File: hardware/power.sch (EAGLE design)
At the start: 31 parts, among them IC3 LM2937, U1 LM324D, U2 LM324D

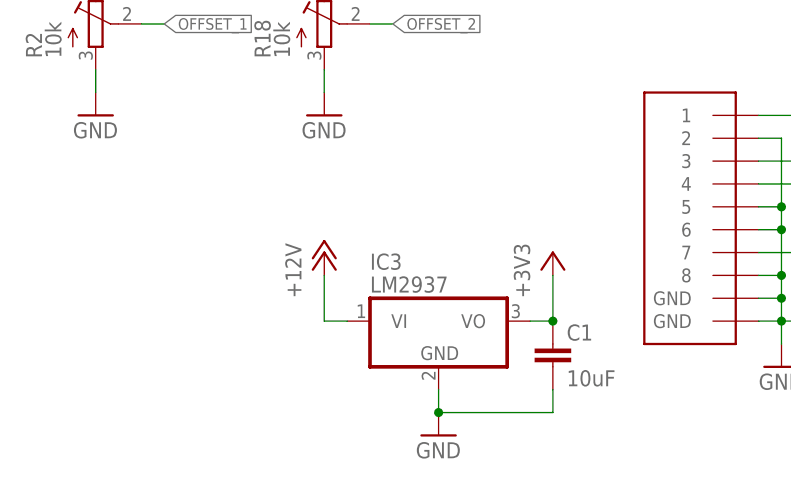
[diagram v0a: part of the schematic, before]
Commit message: preliminary placement and routing
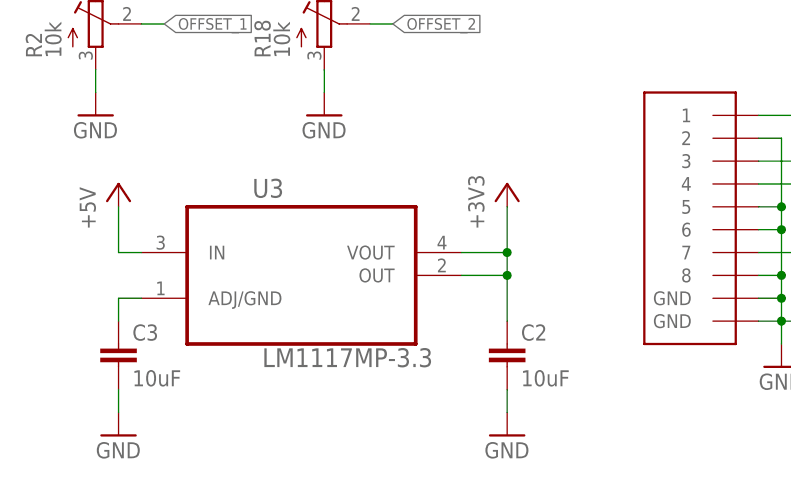
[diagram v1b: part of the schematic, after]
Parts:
- removed C1: 10uF, rcl:C-EUC0805
- removed IC3: LM2937, linear:LM2937
- added C2, C3: 10uF, rcl:C-EUC0805
- added U3: LM1117MP-3.3, hexasense:LM1117MP-3.3
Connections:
- removed net +12V: IC3.VI, U$2.I
- new net N$15: C3.1, U3.ADJ/GND
- net +3V3: now also C2.1, U3.OUT, U3.VOUT; no longer C1.1, IC3.VO
- net +5V: now also U$2.I, U3.IN
- net GND: now also C2.2, C3.2; no longer C1.2, IC3.GND
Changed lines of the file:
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@@
 <part name="GND1" library="supply1" deviceset="GND" device=""/>
 <part name="GND2" library="supply1" deviceset="GND" device=""/>
-<part name="GND3" library="supply1" deviceset="GND" device=""/>
 <part name="GND4" library="supply1" deviceset="GND" device=""/>
-<part name="IC3" library="linear" deviceset="LM2937" device=""/>
-<part name="+3V3" library="supply1" deviceset="+3V3" device=""/>
-<part name="P+1" library="supply1" deviceset="+12V" device=""/>
 <part name="R2" library="rcl" deviceset="R-TRIMM" device="T93YB" value="10k"/>
 <part name="R4" library="rcl" deviceset="R-TRIMM" device="T93YB" value="20k"/>
@@
 <part name="TP4" library="testpad" deviceset="TP" device="B1,27"/>
 <part name="U$2" library="Ergaenzung" deviceset="HOHLBUCHSE" device=""/>
-<part name="P+2" library="supply1" deviceset="+5V" device=""/>
 <part name="GND8" library="supply1" deviceset="GND" device=""/>
 <part name="+3V5" library="supply1" deviceset="+3V3" device=""/>
 <part name="JP2" library="pinhead" deviceset="PINHD-1X4" device="/90"/>
-<part name="C1" library="rcl" deviceset="C-EU" device="C0805" value="10uF"/>
 <part name="U1" library="hexasense" deviceset="LM324D" device=""/>
 <part name="+3V4" library="supply1" deviceset="+3V3" device=""/>
@@
 <part name="GND13" library="supply1" deviceset="GND" device=""/>
 <part name="P+3" library="supply1" deviceset="+5V" device=""/>
+<part name="U3" library="hexasense" deviceset="LM1117MP-3.3" device=""/>
+<part name="P+4" library="supply1" deviceset="+5V" device=""/>
+<part name="+3V9" library="supply1" deviceset="+3V3" device=""/>
+<part name="GND7" library="supply1" deviceset="GND" device=""/>
+<part name="GND14" library="supply1" deviceset="GND" device=""/>
+<part name="C2" library="rcl" deviceset="C-EU" device="C0805" value="10uF"/>
+<part name="C3" library="rcl" deviceset="C-EU" device="C0805" value="10uF"/>
+<part name="P+1" library="supply1" deviceset="+5V" device=""/>
 </parts>
 <sheets>
@@
 <instance part="GND1" gate="1" x="58.42" y="55.88"/>
 <instance part="GND2" gate="1" x="147.32" y="53.34"/>
-<instance part="GND3" gate="1" x="43.18" y="-2.54"/>
 <instance part="GND4" gate="1" x="10.16" y="76.2"/>
-<instance part="IC3" gate="G$1" x="43.18" y="10.16"/>
-<instance part="+3V3" gate="G$1" x="55.88" y="17.78"/>
-<instance part="P+1" gate="1" x="30.48" y="17.78"/>
 <instance part="R2" gate="G$1" x="5.08" y="43.18"/>
 <instance part="R4" gate="G$1" x="147.32" y="63.5" rot="R180"/>
@@
 <instance part="TP4" gate="G$1" x="83.82" y="38.1"/>
 <instance part="U$2" gate="G$1" x="129.54" y="38.1" rot="R180"/>
-<instance part="P+2" gate="1" x="114.3" y="45.72"/>
 <instance part="GND8" gate="1" x="114.3" y="30.48"/>
 <instance part="+3V5" gate="G$1" x="91.44" y="38.1"/>
 <instance part="JP2" gate="A" x="0" y="86.36" rot="R180"/>
-<instance part="C1" gate="G$1" x="55.88" y="7.62"/>
 <instance part="U1" gate="A" x="109.22" y="83.82"/>
 <instance part="+3V4" gate="G$1" x="91.44" y="111.76"/>
@@
 <instance part="GND13" gate="1" x="30.48" y="33.02"/>
 <instance part="P+3" gate="1" x="91.44" y="22.86"/>
+<instance part="U3" gate="A" x="27.94" y="17.78"/>
+<instance part="P+4" gate="1" x="7.62" y="25.4"/>
+<instance part="+3V9" gate="G$1" x="50.8" y="25.4"/>
+<instance part="GND7" gate="1" x="7.62" y="-2.54"/>
+<instance part="GND14" gate="1" x="50.8" y="-2.54"/>
+<instance part="C2" gate="G$1" x="50.8" y="7.62"/>
+<instance part="C3" gate="G$1" x="7.62" y="7.62"/>
+<instance part="P+1" gate="1" x="114.3" y="45.72"/>
 </instances>
 <busses>
@@
 <pinref part="R3" gate="G$1" pin="2"/>
 <pinref part="+3V2" gate="G$1" pin="+3V3"/>
-</segment>
-<segment>
-<wire x1="53.34" y1="10.16" x2="55.88" y2="10.16" width="0.1524" layer="91"/>
-<wire x1="55.88" y1="10.16" x2="55.88" y2="15.24" width="0.1524" layer="91"/>
-<junction x="55.88" y="10.16"/>
-<pinref part="IC3" gate="G$1" pin="VO"/>
-<pinref part="+3V3" gate="G$1" pin="+3V3"/>
-<pinref part="C1" gate="G$1" pin="1"/>
 </segment>
 <segment>
@@
 <pinref part="+3V8" gate="G$1" pin="+3V3"/>
 </segment>
+<segment>
+<pinref part="U3" gate="A" pin="VOUT"/>
+<pinref part="+3V9" gate="G$1" pin="+3V3"/>
+<wire x1="45.72" y1="17.78" x2="50.8" y2="17.78" width="0.1524" layer="91"/>
+<wire x1="50.8" y1="17.78" x2="50.8" y2="22.86" width="0.1524" layer="91"/>
+<pinref part="U3" gate="A" pin="OUT"/>
+<wire x1="45.72" y1="15.24" x2="50.8" y2="15.24" width="0.1524" layer="91"/>
+<wire x1="50.8" y1="15.24" x2="50.8" y2="17.78" width="0.1524" layer="91"/>
+<junction x="50.8" y="17.78"/>
+<pinref part="C2" gate="G$1" pin="1"/>
+<wire x1="50.8" y1="15.24" x2="50.8" y2="10.16" width="0.1524" layer="91"/>
+<junction x="50.8" y="15.24"/>
+</segment>
 </net>
 <net name="GND" class="0">
@@
 <pinref part="R5" gate="G$1" pin="1"/>
 <pinref part="GND1" gate="1" pin="GND"/>
-</segment>
-<segment>
-<wire x1="43.18" y1="0" x2="43.18" y2="2.54" width="0.1524" layer="91"/>
-<wire x1="55.88" y1="2.54" x2="55.88" y2="0" width="0.1524" layer="91"/>
-<wire x1="55.88" y1="0" x2="43.18" y2="0" width="0.1524" layer="91"/>
-<junction x="43.18" y="0"/>
-<pinref part="IC3" gate="G$1" pin="GND"/>
-<pinref part="GND3" gate="1" pin="GND"/>
-<pinref part="C1" gate="G$1" pin="2"/>
 </segment>
 <segment>
@@
 <pinref part="R18" gate="G$1" pin="A"/>
 </segment>
-</net>
-<net name="+12V" class="0">
-<segment>
-<wire x1="33.02" y1="10.16" x2="30.48" y2="10.16" width="0.1524" layer="91"/>
-<wire x1="30.48" y1="10.16" x2="30.48" y2="15.24" width="0.1524" layer="91"/>
-<pinref part="IC3" gate="G$1" pin="VI"/>
-<pinref part="P+1" gate="1" pin="+12V"/>
-</segment>
-<segment>
-<wire x1="116.84" y1="40.64" x2="114.3" y2="40.64" width="0.1524" layer="91"/>
-<wire x1="114.3" y1="40.64" x2="114.3" y2="43.18" width="0.1524" layer="91"/>
-<pinref part="U$2" gate="G$1" pin="I"/>
-<pinref part="P+2" gate="1" pin="+5V"/>
+<segment>
+<pinref part="C2" gate="G$1" pin="2"/>
+<pinref part="GND14" gate="1" pin="GND"/>
+<wire x1="50.8" y1="2.54" x2="50.8" y2="0" width="0.1524" layer="91"/>
+</segment>
+<segment>
+<pinref part="GND7" gate="1" pin="GND"/>
+<pinref part="C3" gate="G$1" pin="2"/>
+<wire x1="7.62" y1="0" x2="7.62" y2="2.54" width="0.1524" layer="91"/>
 </segment>
 </net>
@@
 <wire x1="91.44" y1="17.78" x2="91.44" y2="20.32" width="0.1524" layer="91"/>
 </segment>
-</net>
+<segment>
+<pinref part="U3" gate="A" pin="IN"/>
+<pinref part="P+4" gate="1" pin="+5V"/>
+<wire x1="10.16" y1="17.78" x2="7.62" y2="17.78" width="0.1524" layer="91"/>
+<wire x1="7.62" y1="17.78" x2="7.62" y2="22.86" width="0.1524" layer="91"/>
+</segment>
+<segment>
+<pinref part="U$2" gate="G$1" pin="I"/>
+<pinref part="P+1" gate="1" pin="+5V"/>
+<wire x1="116.84" y1="40.64" x2="114.3" y2="40.64" width="0.1524" layer="91"/>
+<wire x1="114.3" y1="40.64" x2="114.3" y2="43.18" width="0.1524" layer="91"/>
+</segment>
+</net>
+<net name="N$15" class="0">
+<segment>
+<pinref part="U3" gate="A" pin="ADJ/GND"/>
+<pinref part="C3" gate="G$1" pin="1"/>
+<wire x1="10.16" y1="12.7" x2="7.62" y2="12.7" width="0.1524" layer="91"/>
+<wire x1="7.62" y1="12.7" x2="7.62" y2="10.16" width="0.1524" layer="91"/>
+</segment>
+</net>

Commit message: now passing the DRC
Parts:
- added OFFSET-1, OFFSET-2, PT100-1, PT100-2: TPB1,27, testpad:TPB1,27
- renumbered C3 to C1, TP1 to U_M-1, TP2 to TEMP-1, TP3 to GND, TP4 to VCC, TP5 to U_M-2, TP6 to TEMP-2
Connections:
- net OFFSET_1: now also OFFSET-1.TP
- net OFFSET_2: now also OFFSET-2.TP
- net PT100_1: now also PT100-1.TP
- net PT100_2: now also PT100-2.TP
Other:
- moved on the sheet: JP2
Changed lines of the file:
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@@
 <part name="U$1" library="Reichelt" deviceset="MEBP8-8G" device=""/>
 <part name="GND6" library="supply1" deviceset="GND" device=""/>
-<part name="TP1" library="testpad" deviceset="TP" device="B1,27"/>
-<part name="TP2" library="testpad" deviceset="TP" device="B1,27"/>
-<part name="TP3" library="testpad" deviceset="TP" device="B1,27"/>
-<part name="TP4" library="testpad" deviceset="TP" device="B1,27"/>
+<part name="U_M-1" library="testpad" deviceset="TP" device="B1,27"/>
+<part name="TEMP-1" library="testpad" deviceset="TP" device="B1,27"/>
+<part name="GND" library="testpad" deviceset="TP" device="B1,27"/>
+<part name="VCC" library="testpad" deviceset="TP" device="B1,27"/>
 <part name="U$2" library="Ergaenzung" deviceset="HOHLBUCHSE" device=""/>
 <part name="GND8" library="supply1" deviceset="GND" device=""/>
@@
 <part name="GND11" library="supply1" deviceset="GND" device=""/>
 <part name="R16" library="rcl" deviceset="R-TRIMM" device="T93YB" value="20k"/>
-<part name="TP5" library="testpad" deviceset="TP" device="B1,27"/>
-<part name="TP6" library="testpad" deviceset="TP" device="B1,27"/>
+<part name="U_M-2" library="testpad" deviceset="TP" device="B1,27"/>
+<part name="TEMP-2" library="testpad" deviceset="TP" device="B1,27"/>
 <part name="U2" library="hexasense" deviceset="LM324D" device=""/>
 <part name="+3V7" library="supply1" deviceset="+3V3" device=""/>
@@
 <part name="GND14" library="supply1" deviceset="GND" device=""/>
 <part name="C2" library="rcl" deviceset="C-EU" device="C0805" value="10uF"/>
-<part name="C3" library="rcl" deviceset="C-EU" device="C0805" value="10uF"/>
+<part name="C1" library="rcl" deviceset="C-EU" device="C0805" value="10uF"/>
 <part name="P+1" library="supply1" deviceset="+5V" device=""/>
+<part name="OFFSET-1" library="testpad" deviceset="TP" device="B1,27"/>
+<part name="OFFSET-2" library="testpad" deviceset="TP" device="B1,27"/>
+<part name="PT100-2" library="testpad" deviceset="TP" device="B1,27"/>
+<part name="PT100-1" library="testpad" deviceset="TP" device="B1,27"/>
 </parts>
 <sheets>
@@
 <instance part="GND1" gate="1" x="58.42" y="55.88"/>
 <instance part="GND2" gate="1" x="147.32" y="53.34"/>
-<instance part="GND4" gate="1" x="10.16" y="76.2"/>
+<instance part="GND4" gate="1" x="0" y="78.74"/>
 <instance part="R2" gate="G$1" x="5.08" y="43.18"/>
 <instance part="R4" gate="G$1" x="147.32" y="63.5" rot="R180"/>
@@
 <instance part="U$1" gate="G$1" x="71.12" y="22.86"/>
 <instance part="GND6" gate="1" x="81.28" y="5.08"/>
-<instance part="TP1" gate="G$1" x="134.62" y="99.06"/>
-<instance part="TP2" gate="G$1" x="147.32" y="99.06"/>
-<instance part="TP3" gate="G$1" x="93.98" y="15.24"/>
-<instance part="TP4" gate="G$1" x="83.82" y="38.1"/>
+<instance part="U_M-1" gate="G$1" x="134.62" y="99.06"/>
+<instance part="TEMP-1" gate="G$1" x="147.32" y="99.06"/>
+<instance part="GND" gate="G$1" x="93.98" y="15.24"/>
+<instance part="VCC" gate="G$1" x="83.82" y="38.1"/>
 <instance part="U$2" gate="G$1" x="129.54" y="38.1" rot="R180"/>
 <instance part="GND8" gate="1" x="114.3" y="30.48"/>
 <instance part="+3V5" gate="G$1" x="91.44" y="38.1"/>
-<instance part="JP2" gate="A" x="0" y="86.36" rot="R180"/>
+<instance part="JP2" gate="A" x="-10.16" y="88.9" rot="R180"/>
 <instance part="U1" gate="A" x="109.22" y="83.82"/>
 <instance part="+3V4" gate="G$1" x="91.44" y="111.76"/>
@@
 <instance part="GND11" gate="1" x="147.32" y="124.46"/>
 <instance part="R16" gate="G$1" x="147.32" y="134.62" rot="R180"/>
-<instance part="TP5" gate="G$1" x="134.62" y="170.18"/>
-<instance part="TP6" gate="G$1" x="147.32" y="170.18"/>
+<instance part="U_M-2" gate="G$1" x="134.62" y="170.18"/>
+<instance part="TEMP-2" gate="G$1" x="147.32" y="170.18"/>
 <instance part="U2" gate="A" x="109.22" y="154.94"/>
 <instance part="+3V7" gate="G$1" x="91.44" y="182.88"/>
@@
 <instance part="GND14" gate="1" x="50.8" y="-2.54"/>
 <instance part="C2" gate="G$1" x="50.8" y="7.62"/>
-<instance part="C3" gate="G$1" x="7.62" y="7.62"/>
+<instance part="C1" gate="G$1" x="7.62" y="7.62"/>
 <instance part="P+1" gate="1" x="114.3" y="45.72"/>
+<instance part="OFFSET-1" gate="G$1" x="12.7" y="50.8"/>
+<instance part="OFFSET-2" gate="G$1" x="38.1" y="50.8"/>
+<instance part="PT100-2" gate="G$1" x="2.54" y="93.98"/>
+<instance part="PT100-1" gate="G$1" x="7.62" y="93.98"/>
 </instances>
 <busses>
@@
 <wire x1="83.82" y1="33.02" x2="83.82" y2="35.56" width="0.1524" layer="91"/>
 <junction x="83.82" y="33.02"/>
-<pinref part="TP4" gate="G$1" pin="TP"/>
+<pinref part="VCC" gate="G$1" pin="TP"/>
 <pinref part="U$1" gate="G$1" pin="1"/>
 <pinref part="+3V5" gate="G$1" pin="+3V3"/>
@@
 </segment>
 <segment>
-<wire x1="10.16" y1="78.74" x2="10.16" y2="83.82" width="0.1524" layer="91"/>
-<wire x1="10.16" y1="83.82" x2="10.16" y2="88.9" width="0.1524" layer="91"/>
-<wire x1="10.16" y1="88.9" x2="2.54" y2="88.9" width="0.1524" layer="91"/>
-<wire x1="2.54" y1="83.82" x2="10.16" y2="83.82" width="0.1524" layer="91"/>
-<junction x="10.16" y="83.82"/>
+<wire x1="0" y1="81.28" x2="0" y2="86.36" width="0.1524" layer="91"/>
+<wire x1="0" y1="86.36" x2="0" y2="91.44" width="0.1524" layer="91"/>
+<wire x1="0" y1="91.44" x2="-7.62" y2="91.44" width="0.1524" layer="91"/>
+<wire x1="-7.62" y1="86.36" x2="0" y2="86.36" width="0.1524" layer="91"/>
+<junction x="0" y="86.36"/>
 <pinref part="JP2" gate="A" pin="4"/>
 <pinref part="GND4" gate="1" pin="GND"/>
@@
 <wire x1="78.74" y1="20.32" x2="81.28" y2="20.32" width="0.1524" layer="91"/>
 <junction x="81.28" y="20.32"/>
-<pinref part="TP3" gate="G$1" pin="TP"/>
+<pinref part="GND" gate="G$1" pin="TP"/>
 <wire x1="93.98" y1="12.7" x2="93.98" y2="10.16" width="0.1524" layer="91"/>
 <wire x1="93.98" y1="10.16" x2="81.28" y2="10.16" width="0.1524" layer="91"/>
@@
 <segment>
 <pinref part="GND7" gate="1" pin="GND"/>
-<pinref part="C3" gate="G$1" pin="2"/>
+<pinref part="C1" gate="G$1" pin="2"/>
 <wire x1="7.62" y1="0" x2="7.62" y2="2.54" width="0.1524" layer="91"/>
 </segment>
@@
 </segment>
 <segment>
-<wire x1="2.54" y1="86.36" x2="12.7" y2="86.36" width="0.1524" layer="91"/>
-<label x="12.7" y="86.36" size="1.27" layer="95" xref="yes"/>
+<wire x1="-7.62" y1="88.9" x2="2.54" y2="88.9" width="0.1524" layer="91"/>
+<label x="10.16" y="88.9" size="1.27" layer="95" xref="yes"/>
 <pinref part="JP2" gate="A" pin="3"/>
+<pinref part="PT100-2" gate="G$1" pin="TP"/>
+<wire x1="2.54" y1="88.9" x2="10.16" y2="88.9" width="0.1524" layer="91"/>
+<wire x1="2.54" y1="91.44" x2="2.54" y2="88.9" width="0.1524" layer="91"/>
+<junction x="2.54" y="88.9"/>
 </segment>
 </net>
@@
 <label x="12.7" y="43.18" size="1.27" layer="95" xref="yes"/>
 <pinref part="R2" gate="G$1" pin="S"/>
+<pinref part="OFFSET-1" gate="G$1" pin="TP"/>
+<wire x1="12.7" y1="43.18" x2="12.7" y2="48.26" width="0.1524" layer="91"/>
 </segment>
 <segment>
@@
 <label x="38.1" y="43.18" size="1.27" layer="95" xref="yes"/>
 <pinref part="R18" gate="G$1" pin="S"/>
+<pinref part="OFFSET-2" gate="G$1" pin="TP"/>
+<wire x1="38.1" y1="43.18" x2="38.1" y2="48.26" width="0.1524" layer="91"/>
 </segment>
 <segment>
@@
 <net name="PT100_1" class="0">
 <segment>
-<wire x1="2.54" y1="81.28" x2="12.7" y2="81.28" width="0.1524" layer="91"/>
-<label x="12.7" y="81.28" size="1.27" layer="95" xref="yes"/>
+<wire x1="-7.62" y1="83.82" x2="7.62" y2="83.82" width="0.1524" layer="91"/>
+<label x="10.16" y="83.82" size="1.27" layer="95" xref="yes"/>
 <pinref part="JP2" gate="A" pin="1"/>
+<pinref part="PT100-1" gate="G$1" pin="TP"/>
+<wire x1="7.62" y1="83.82" x2="10.16" y2="83.82" width="0.1524" layer="91"/>
+<wire x1="7.62" y1="91.44" x2="7.62" y2="83.82" width="0.1524" layer="91"/>
+<junction x="7.62" y="83.82"/>
 </segment>
 <segment>
@@
 <label x="139.7" y="160.02" size="1.27" layer="95" xref="yes"/>
 <pinref part="U2" gate="A" pin="OUT3"/>
-<pinref part="TP5" gate="G$1" pin="TP"/>
+<pinref part="U_M-2" gate="G$1" pin="TP"/>
 </segment>
 <segment>
@@
 <label x="139.7" y="88.9" size="1.27" layer="95" xref="yes"/>
 <pinref part="U1" gate="A" pin="OUT3"/>
-<pinref part="TP1" gate="G$1" pin="TP"/>
+<pinref part="U_M-1" gate="G$1" pin="TP"/>
 </segment>
 <segment>
@@
 <label x="147.32" y="157.48" size="1.27" layer="95" xref="yes"/>
 <pinref part="R15" gate="G$1" pin="1"/>
-<pinref part="TP6" gate="G$1" pin="TP"/>
+<pinref part="TEMP-2" gate="G$1" pin="TP"/>
 <pinref part="U2" gate="A" pin="OUT4"/>
 </segment>
@@
 <label x="147.32" y="86.36" size="1.27" layer="95" xref="yes"/>
 <pinref part="R9" gate="G$1" pin="1"/>
-<pinref part="TP2" gate="G$1" pin="TP"/>
+<pinref part="TEMP-1" gate="G$1" pin="TP"/>
 <pinref part="U1" gate="A" pin="OUT4"/>
 </segment>
@@
 <segment>
 <pinref part="U3" gate="A" pin="ADJ/GND"/>
-<pinref part="C3" gate="G$1" pin="1"/>
+<pinref part="C1" gate="G$1" pin="1"/>
 <wire x1="10.16" y1="12.7" x2="7.62" y2="12.7" width="0.1524" layer="91"/>
 <wire x1="7.62" y1="12.7" x2="7.62" y2="10.16" width="0.1524" layer="91"/>

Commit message: changed testpads to THT
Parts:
- GND, OFFSET-1, OFFSET-2, PT100-1, PT100-2, TEMP-1, TEMP-2, U_M-1, U_M-2, VCC: value TPB1,27 -> TPPAD1-13; device testpad:TPB1,27 -> testpad:TPPAD1-13
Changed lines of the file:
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@@
 <part name="U$1" library="Reichelt" deviceset="MEBP8-8G" device=""/>
 <part name="GND6" library="supply1" deviceset="GND" device=""/>
-<part name="U_M-1" library="testpad" deviceset="TP" device="B1,27"/>
-<part name="TEMP-1" library="testpad" deviceset="TP" device="B1,27"/>
-<part name="GND" library="testpad" deviceset="TP" device="B1,27"/>
-<part name="VCC" library="testpad" deviceset="TP" device="B1,27"/>
+<part name="U_M-1" library="testpad" deviceset="TP" device="PAD1-13" value="TPPAD1-13"/>
+<part name="TEMP-1" library="testpad" deviceset="TP" device="PAD1-13" value="TPPAD1-13"/>
+<part name="GND" library="testpad" deviceset="TP" device="PAD1-13" value="TPPAD1-13"/>
+<part name="VCC" library="testpad" deviceset="TP" device="PAD1-13" value="TPPAD1-13"/>
 <part name="U$2" library="Ergaenzung" deviceset="HOHLBUCHSE" device=""/>
 <part name="GND8" library="supply1" deviceset="GND" device=""/>
@@
 <part name="GND11" library="supply1" deviceset="GND" device=""/>
 <part name="R16" library="rcl" deviceset="R-TRIMM" device="T93YB" value="20k"/>
-<part name="U_M-2" library="testpad" deviceset="TP" device="B1,27"/>
-<part name="TEMP-2" library="testpad" deviceset="TP" device="B1,27"/>
+<part name="U_M-2" library="testpad" deviceset="TP" device="PAD1-13" value="TPPAD1-13"/>
+<part name="TEMP-2" library="testpad" deviceset="TP" device="PAD1-13" value="TPPAD1-13"/>
 <part name="U2" library="hexasense" deviceset="LM324D" device=""/>
 <part name="+3V7" library="supply1" deviceset="+3V3" device=""/>
@@
 <part name="C1" library="rcl" deviceset="C-EU" device="C0805" value="10uF"/>
 <part name="P+1" library="supply1" deviceset="+5V" device=""/>
-<part name="OFFSET-1" library="testpad" deviceset="TP" device="B1,27"/>
-<part name="OFFSET-2" library="testpad" deviceset="TP" device="B1,27"/>
-<part name="PT100-2" library="testpad" deviceset="TP" device="B1,27"/>
-<part name="PT100-1" library="testpad" deviceset="TP" device="B1,27"/>
+<part name="OFFSET-1" library="testpad" deviceset="TP" device="PAD1-13" value="TPPAD1-13"/>
+<part name="OFFSET-2" library="testpad" deviceset="TP" device="PAD1-13" value="TPPAD1-13"/>
+<part name="PT100-2" library="testpad" deviceset="TP" device="PAD1-13" value="TPPAD1-13"/>
+<part name="PT100-1" library="testpad" deviceset="TP" device="PAD1-13" value="TPPAD1-13"/>
 </parts>
 <sheets>
